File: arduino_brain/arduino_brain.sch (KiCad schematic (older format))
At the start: 52 parts, among them Q1 2N3904, Q10 2N3904, Q11 2N3906, Q2 TIP120, Q3 TIP120, Q4 2N3904, Q5 2N3906, Q6 2N3904, Q7 2N3906, Q8 2N3904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

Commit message: Cleaned up Arduino board connections
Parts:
- added R?: 10k, symbol Device:R
- added R?: 2k7, symbol Device:R_Small
- added TH?: Thermistor, symbol Device:Thermistor
- R11, R13: value 4k7 -> CFR16-4k7
- R12: value 1k -> CFR16-1k0
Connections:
- net +5V: now also R?.1, TH?.1
- net -BATT: now also R?.2
- net A1_A0: now also R?.1, TH?.2; no longer R?.1
- net A1_D4: now also R?.2; no longer R7.2
- net A1_D5: now also R7.2
- new net A2_A0: R?.1
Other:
- note added: "TIP120:\nDT_meas = 15.74 - 12.5 = 3.2 degC\nDU_horn = ? V (multimeter not able to read -> going to 1 when applying load). DU_CE = 0.7 V\nI_in_meas@12 V = ~1 A (oscillating fast)"
- note added: "TODO: measure for light beam, check that it will not over-heat."
- note added: "V_brake = 11.78 V —> P_dis = 0.22*0.1 = 22 mW —> DT_theo = 3.5 degC"
- note added: "soft horn"
- note added: "thermistor"
- note removed: "TIP120:\nDT_meas = 15.74 - 12.5 = 3.2 degC\nDU_horn = ? V (multimeter not able to read -> going to 1 when applying load)\nI_in_meas@12 V = ~1 A (oscillating fast)"
- note removed: "TODO: measure for light beam"
- moved on the sheet: R7
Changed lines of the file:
@@
 P 4800 1650
 F 0 "R11" V 5007 1650 50  0000 C CNN
-F 1 "4k7" V 4916 1650 50  0000 C CNN
+F 1 "CFR16-4k7" V 4916 1650 50  0000 C CNN
 F 2 "" V 4730 1650 50  0001 C CNN
 F 3 "~" H 4800 1650 50  0001 C CNN
@@
 P 5850 1450
 F 0 "R12" V 6057 1450 50  0000 C CNN
-F 1 "1k" V 5966 1450 50  0000 C CNN
+F 1 "CFR16-1k0" V 5966 1450 50  0000 C CNN
 F 2 "" V 5780 1450 50  0001 C CNN
 F 3 "~" H 5850 1450 50  0001 C CNN
@@
 P 5850 1150
 F 0 "R13" V 6057 1150 50  0000 C CNN
-F 1 "4k7" V 5966 1150 50  0000 C CNN
+F 1 "CFR16-4k7" V 5966 1150 50  0000 C CNN
 F 2 "" V 5780 1150 50  0001 C CNN
 F 3 "~" H 5850 1150 50  0001 C CNN
@@
 L Device:R R7
 U 1 1 5E1687C7
-P 2650 6600
-F 0 "R7" V 2857 6600 50  0000 C CNN
-F 1 "10k" V 2766 6600 50  0000 C CNN
-F 2 "" V 2580 6600 50  0001 C CNN
-F 3 "~" H 2650 6600 50  0001 C CNN
-	1    2650 6600
-	1    0    0    -1
-$EndComp
-Wire Wire Line
-	2350 6450 2650 6450
+P 2950 6600
+F 0 "R7" V 3157 6600 50  0000 C CNN
+F 1 "10k" V 3066 6600 50  0000 C CNN
+F 2 "" V 2880 6600 50  0001 C CNN
+F 3 "~" H 2950 6600 50  0001 C CNN
+	1    2950 6600
+	1    0    0    -1
+$EndComp
 $Comp
 L Device:R R5
@@
 Wire Wire Line
 	2050 6450 2350 6450
-Connection ~ 2350 6450
 $Comp
 L Device:R R4
@@
 (2?) Blue
 Text GLabel 1300 3600 2    50   Input ~ 0
-A1_A1
+A2_D5
 Wire Wire Line
 	1250 3400 1250 3600
@@
 Text GLabel 5400 6650 0    50   Output ~ 0
 A1_D2
-Text GLabel 2750 6850 2    50   Output ~ 0
+Text GLabel 3050 6850 2    50   Output ~ 0
 A1_D0
-Text GLabel 2750 7000 2    50   Output ~ 0
+Text GLabel 3050 7000 2    50   Output ~ 0
 A1_D1
 Text GLabel 5400 6850 0    50   Output ~ 0
 A1_D4
-Text GLabel 2750 7150 2    50   Output ~ 0
+Text GLabel 3050 7150 2    50   Output ~ 0
 A1_D2
 Text GLabel 5400 7150 0    50   Output ~ 0
 A1_D7
-Text GLabel 2750 7300 2    50   Output ~ 0
+Text GLabel 3050 7300 2    50   Output ~ 0
 A1_D4
 Text GLabel 5400 7250 0    50   Output ~ 0
@@
 	1350 7150 2350 7150
 Wire Wire Line
-	1350 7300 2650 7300
-Wire Wire Line
 	1750 6450 1750 6400
 Connection ~ 1750 6450
 Wire Wire Line
 	1750 6750 1750 6850
-Connection ~ 1750 6850
-Wire Wire Line
-	1750 6850 2750 6850
-Wire Wire Line
-	2050 6750 2050 7000
-Connection ~ 2050 7000
-Wire Wire Line
-	2050 7000 2750 7000
-Wire Wire Line
-	2350 6750 2350 7150
-Connection ~ 2350 7150
-Wire Wire Line
-	2350 7150 2750 7150
-Wire Wire Line
-	2650 6750 2650 7300
-Connection ~ 2650 7300
-Wire Wire Line
-	2650 7300 2750 7300
 $Comp
 L Device:R R?
@@
 	1300 4800 1300 4900
 Text GLabel 1000 5300 0    50   Input ~ 0
-A1_A0
+A2_A0
 $Comp
 L power:GND #PWR?
@@
 Text Notes 5050 7800 2    50   ~ 0
 Screen
-Text Notes 7550 7100 2    50   ~ 0
+Text Notes -550 6050 2    50   ~ 0
 battery
 Text GLabel 5400 6550 0    50   Output ~ 0
@@
 Text Notes 5050 7700 2    50   ~ 0
 brakes
-Text Notes 7500 7200 2    50   ~ 0
+Text Notes -2350 5950 2    50   ~ 0
 speed
 Text GLabel 900  4150 0    50   Output ~ 0
@@
 12 to 7 V buck converter measurements of consumption / temperature:\n1. load = 5100 Ohm: U_out = 7V, I_out,calc = 1.4 mA, U_in = 12V, I_in = 8 mA ==> efficicency 10 %, P_dissipated = 86.4 mW, DT_meas = 1.1 degC, DT_theo = 4.3 degC\n2. load = Arduino Uno R3, U_out = 7V, I_out_meas = 50 mA, U_in = 12V, I_in = 45 mA ==> efficiency 65%, P_dissipated = 189 mW, DT_meas = 3.6 degC, DT_theo = 9.45 degC\n3. load = Arduino Uno R3 w/ BLE and SIM808 Shield (off): U_out = 7V, I_out_meas = 57 mA, U_in = 12V, I_in = 50 mA ==> efficiency 67%, P_dissipated = 198 mW\n4. load = Arduino Uno R3 w/ BLE and SIM808 Shield (on): U_out = 7V, I_out_meas = 70 mA, U_in = 12V, I_in = 55 mA ==> efficiency 74 %, P_dissipated = 172 mW, DT_meas = 4 degC
 Text Notes 7750 4600 0    50   ~ 0
-TIP120:\nDT_meas = 15.74 - 12.5 = 3.2 degC\nDU_horn = ? V (multimeter not able to read -> going to 1 when applying load)\nI_in_meas@12 V = ~1 A (oscillating fast)
+TIP120:\nDT_meas = 15.74 - 12.5 = 3.2 degC\nDU_horn = ? V (multimeter not able to read -> going to 1 when applying load). DU_CE = 0.7 V\nI_in_meas@12 V = ~1 A (oscillating fast)
 Text Notes 8050 3700 0    50   ~ 0
-TODO: measure for light beam
+TODO: measure for light beam, check that it will not over-heat.
 Text Notes 7750 4100 0    50   ~ 0
 TIP120:\nDT_meas = xx - yy = zz degC\nDU_horn = ? V (multimeter not able to read -> going to 1 when applying load)\nI_in_meas@12 V = ~1 A (oscillating fast)
+Text Notes 4750 7000 0    50   ~ 0
+soft horn
+$Comp
+L Device:R R?
+U 1 1 5E3DD171
+P 2650 6600
+F 0 "R?" V 2857 6600 50  0000 C CNN
+F 1 "10k" V 2766 6600 50  0000 C CNN
+F 2 "" V 2580 6600 50  0001 C CNN
+F 3 "~" H 2650 6600 50  0001 C CNN
+	1    2650 6600
+	1    0    0    -1
+$EndComp
+Connection ~ 2650 7300
+Wire Wire Line
+	1350 7300 2650 7300
+Wire Wire Line
+	2650 7300 3050 7300
+Wire Wire Line
+	2650 6750 2650 7300
+Wire Wire Line
+	2050 6750 2050 7000
+Wire Wire Line
+	2350 6750 2350 7150
+Wire Wire Line
+	3050 6850 1750 6850
+Connection ~ 1750 6850
+Wire Wire Line
+	3050 7000 2050 7000
+Connection ~ 2050 7000
+Wire Wire Line
+	3050 7150 2350 7150
+Connection ~ 2350 7150
+Text GLabel 3050 7800 2    50   Output ~ 0
+A1_D5
+Text GLabel 1550 7800 0    50   Output ~ 10
+COMMODO_SOFT_HORN
+Wire Wire Line
+	1550 7800 2950 7800
+Wire Wire Line
+	2350 6450 2650 6450
+Connection ~ 2350 6450
+Connection ~ 2650 6450
+Wire Wire Line
+	2650 6450 2950 6450
+Wire Wire Line
+	2950 6750 2950 7800
+Connection ~ 2950 7800
+Wire Wire Line
+	2950 7800 3050 7800
+Text Notes 7950 2300 0    50   ~ 0
+V_brake = 11.78 V —> P_dis = 0.22*0.1 = 22 mW —> DT_theo = 3.5 degC
+Text Notes 7300 7100 0    50   ~ 0
+thermistor
+$Comp
+L Device:R_Small R?
+U 1 1 5E43CFA1
+P 8800 7050
+F 0 "R?" V 9007 7050 50  0000 C CNN
+F 1 "2k7" V 8916 7050 50  0000 C CNN
+F 2 "" V 8730 7050 50  0001 C CNN
+F 3 "~" H 8800 7050 50  0001 C CNN
+	1    8800 7050
+	0    -1   -1   0
+$EndComp
+Text GLabel 8550 7050 0    50   Output ~ 0
+A1_A0
+$Comp
+L power:GND #PWR?
+U 1 1 5E44C1CB
+P 9000 7050
+F 0 "#PWR?" H 9000 6800 50  0001 C CNN
+F 1 "GND" H 9005 6877 50  0000 C CNN
+F 2 "" H 9000 7050 50  0001 C CNN
+F 3 "" H 9000 7050 50  0001 C CNN
+	1    9000 7050
+	1    0    0    -1
+$EndComp
+Wire Wire Line
+	8900 7050 9000 7050
+$Comp
+L Device:Thermistor TH?
+U 1 1 5E45B7DF
+P 8650 6650
+F 0 "TH?" H 8755 6696 50  0000 L CNN
+F 1 "Thermistor" H 8755 6605 50  0000 L CNN
+F 2 "" H 8650 6650 50  0001 C CNN
+F 3 "~" H 8650 6650 50  0001 C CNN
+	1    8650 6650
+	1    0    0    -1
+$EndComp
+Wire Wire Line
+	8550 7050 8650 7050
+Wire Wire Line
+	8650 6850 8650 7050
+Connection ~ 8650 7050
+Wire Wire Line
+	8650 7050 8700 7050
+$Comp
+L power:+5V #PWR?
+U 1 1 5E493EB9
+P 8650 6350
+F 0 "#PWR?" H 8650 6200 50  0001 C CNN
+F 1 "+5V" H 8665 6523 50  0000 C CNN
+F 2 "" H 8650 6350 50  0001 C CNN
+F 3 "" H 8650 6350 50  0001 C CNN
+	1    8650 6350
+	1    0    0    -1
+$EndComp
+Wire Wire Line
+	8650 6350 8650 6450
 $EndSCHEMATC

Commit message: Adapted brake light R values
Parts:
- R11: value CFR16-4k7 -> CFR16-3k3
- R13: value CFR16-4k7 -> CFR16-1k2
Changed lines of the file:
@@
 P 4800 1650
 F 0 "R11" V 5007 1650 50  0000 C CNN
-F 1 "CFR16-4k7" V 4916 1650 50  0000 C CNN
+F 1 "CFR16-3k3" V 4916 1650 50  0000 C CNN
 F 2 "" V 4730 1650 50  0001 C CNN
 F 3 "~" H 4800 1650 50  0001 C CNN
@@
 P 5850 1150
 F 0 "R13" V 6057 1150 50  0000 C CNN
-F 1 "CFR16-4k7" V 5966 1150 50  0000 C CNN
+F 1 "CFR16-1k2" V 5966 1150 50  0000 C CNN
 F 2 "" V 5780 1150 50  0001 C CNN
 F 3 "~" H 5850 1150 50  0001 C CNN

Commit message: Added horn cap
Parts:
- added C?: C320C104M5R5TA, symbol Device:C_Small
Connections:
- net +12V: now also C?.2
- net HORN_GND: now also C?.1
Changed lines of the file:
@@
 	6550 4050 6550 4550
 Wire Wire Line
-	6300 4350 6850 4350
+	6300 4350 6700 4350
 Connection ~ 6850 4350
 Wire Wire Line
@@
 Connection ~ 6850 4550
 Wire Wire Line
-	6850 4550 6550 4550
+	6850 4550 6700 4550
 Connection ~ 4950 4750
 $Comp
@@
 Wire Wire Line
 	8650 6350 8650 6450
+$Comp
+L Device:C_Small C?
+U 1 1 5E4A3740
+P 6700 4450
+F 0 "C?" V 6929 4450 50  0000 C CNN
+F 1 "C320C104M5R5TA" V 6838 4450 50  0000 C CNN
+F 2 "" H 6700 4450 50  0001 C CNN
+F 3 "~" H 6700 4450 50  0001 C CNN
+	1    6700 4450
+	1    0    0    -1
+$EndComp
+Connection ~ 6700 4350
+Wire Wire Line
+	6700 4350 6850 4350
+Connection ~ 6700 4550
+Wire Wire Line
+	6700 4550 6550 4550
 $EndSCHEMATC

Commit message: Removed horn cap
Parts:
- removed C?: C320C104M5R5TA, symbol Device:C_Small
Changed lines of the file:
@@
 Wire Wire Line
 	6550 4050 6550 4550
-Wire Wire Line
-	6300 4350 6700 4350
 Connection ~ 6850 4350
 Wire Wire Line
 	6850 4350 7000 4350
 Connection ~ 6850 4550
-Wire Wire Line
-	6850 4550 6700 4550
 Connection ~ 4950 4750
 $Comp
@@
 Wire Wire Line
 	8650 6350 8650 6450
-$Comp
-L Device:C_Small C?
-U 1 1 5E4A3740
-P 6700 4450
-F 0 "C?" V 6929 4450 50  0000 C CNN
-F 1 "C320C104M5R5TA" V 6838 4450 50  0000 C CNN
-F 2 "" H 6700 4450 50  0001 C CNN
-F 3 "~" H 6700 4450 50  0001 C CNN
-	1    6700 4450
-	1    0    0    -1
-$EndComp
-Connection ~ 6700 4350
-Wire Wire Line
-	6700 4350 6850 4350
-Connection ~ 6700 4550
-Wire Wire Line
-	6700 4550 6550 4550
+Wire Wire Line
+	6300 4350 6850 4350
+Wire Wire Line
+	6550 4550 6850 4550
 $EndSCHEMATC

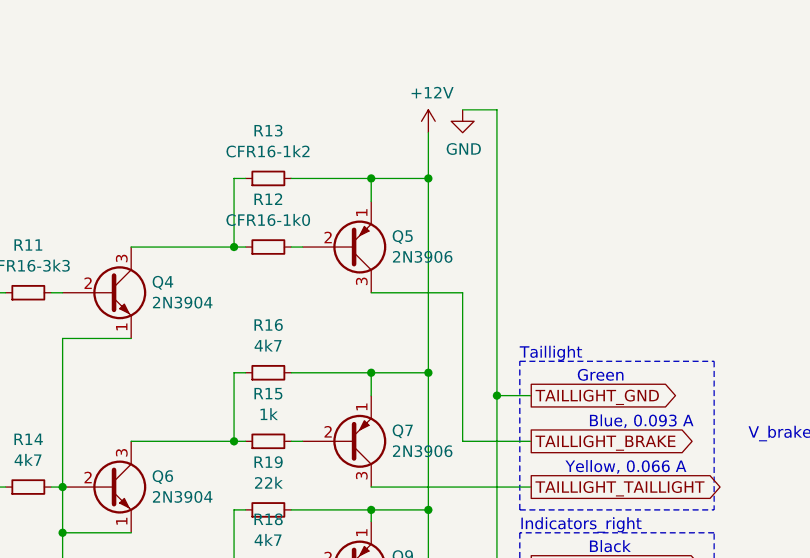
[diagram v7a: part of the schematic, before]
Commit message: Added bypass capacitor near PNP switch
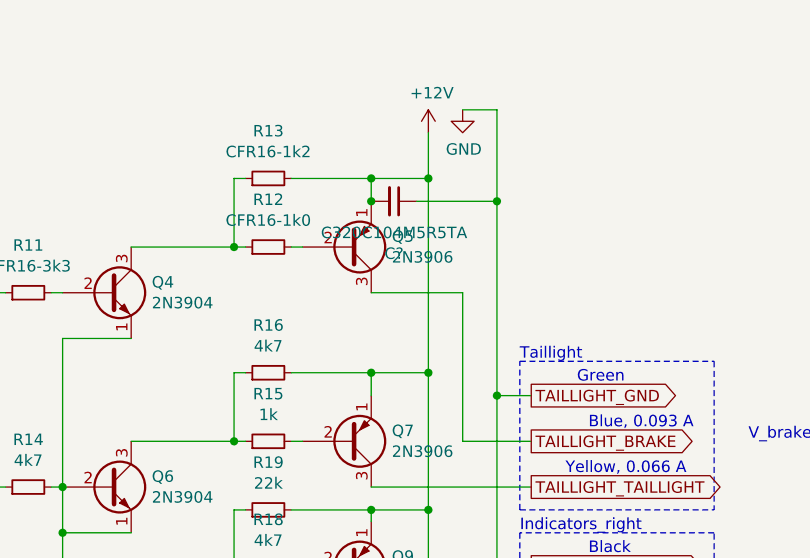
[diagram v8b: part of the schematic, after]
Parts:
- added C?: C320C104M5R5TA, symbol Device:C_Small
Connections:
- net +12V: now also C?.2
- net -BATT: now also C?.1
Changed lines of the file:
@@
 	7000 3400 6850 3400
 Wire Wire Line
-	6850 850  6850 2100
+	6850 850  6850 1250
 Connection ~ 6850 2100
 Wire Wire Line
@@
 Wire Wire Line
 	6550 4550 6850 4550
+$Comp
+L Device:C_Small C?
+U 1 1 5E4F55BB
+P 6400 1250
+F 0 "C?" V 6629 1250 50  0000 C CNN
+F 1 "C320C104M5R5TA" V 6538 1250 50  0000 C CNN
+F 2 "" H 6400 1250 50  0001 C CNN
+F 3 "~" H 6400 1250 50  0001 C CNN
+	1    6400 1250
+	0    1    1    0
+$EndComp
+Connection ~ 6300 1250
+Wire Wire Line
+	6500 1250 6850 1250
+Connection ~ 6850 1250
+Wire Wire Line
+	6850 1250 6850 2100
 $EndSCHEMATC
